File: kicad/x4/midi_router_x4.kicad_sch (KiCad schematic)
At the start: 83 parts, among them J1 USB_B, J11 DIN-5_180degree, J12 DIN-5_180degree, J13 DIN-5_180degree, J14 DIN-5_180degree, J2 Conn_02x03_Odd_Even, J21 DIN-5_180degree, J22 DIN-5_180degree, J23 DIN-5_180degree, J24 DIN-5_180degree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

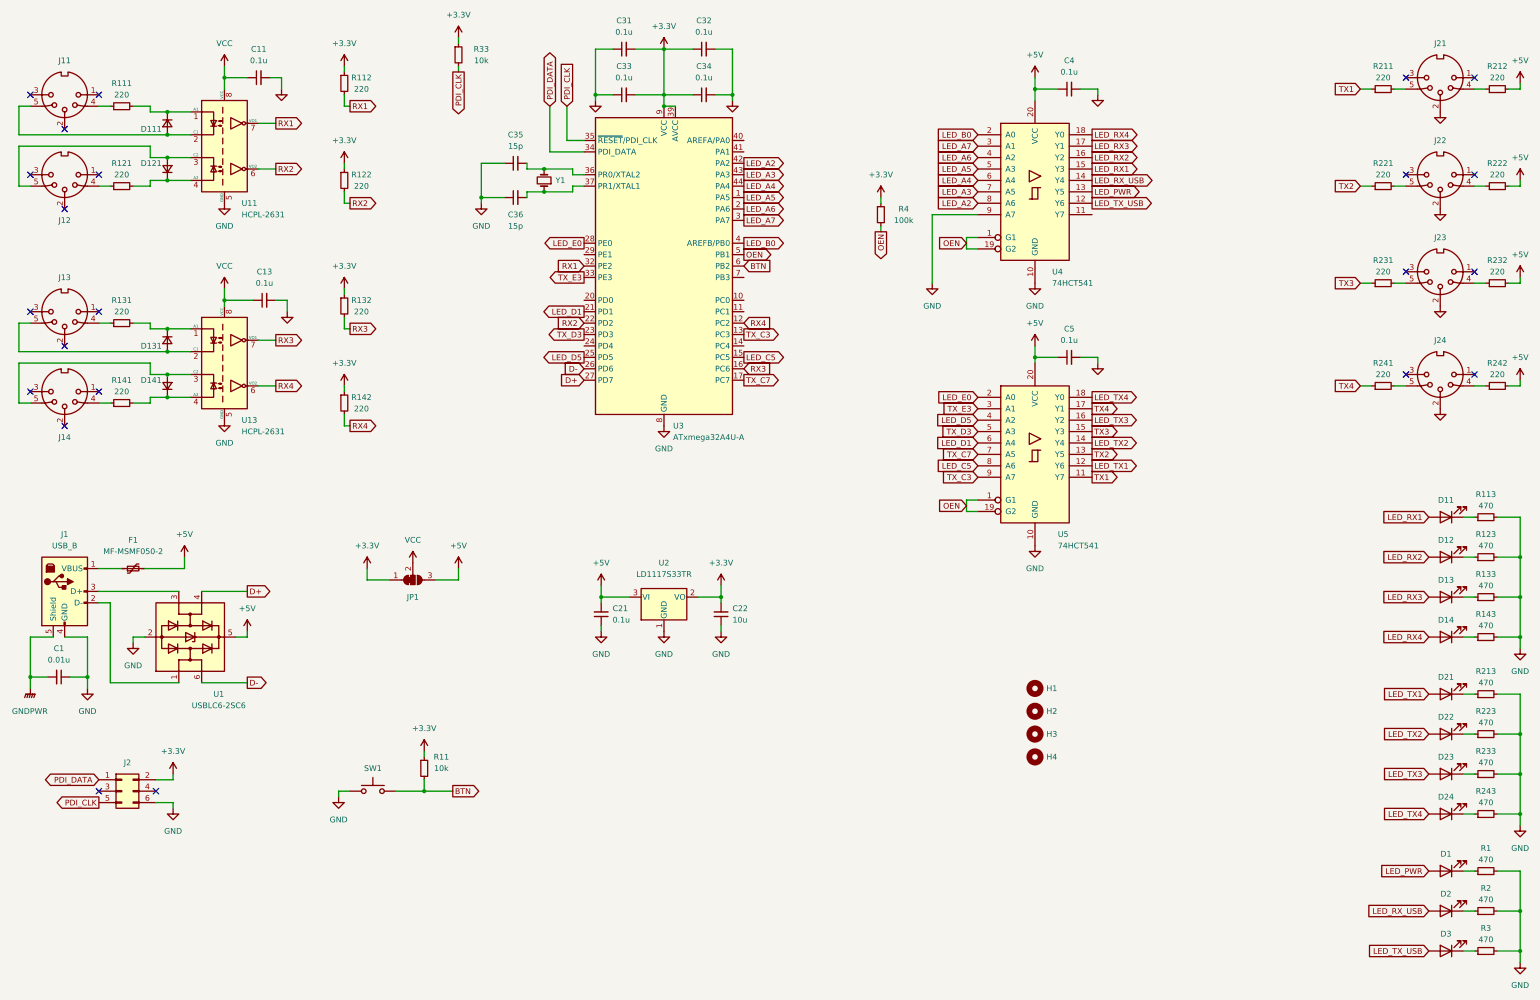
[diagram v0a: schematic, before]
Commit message: x4 KiCad upgrade
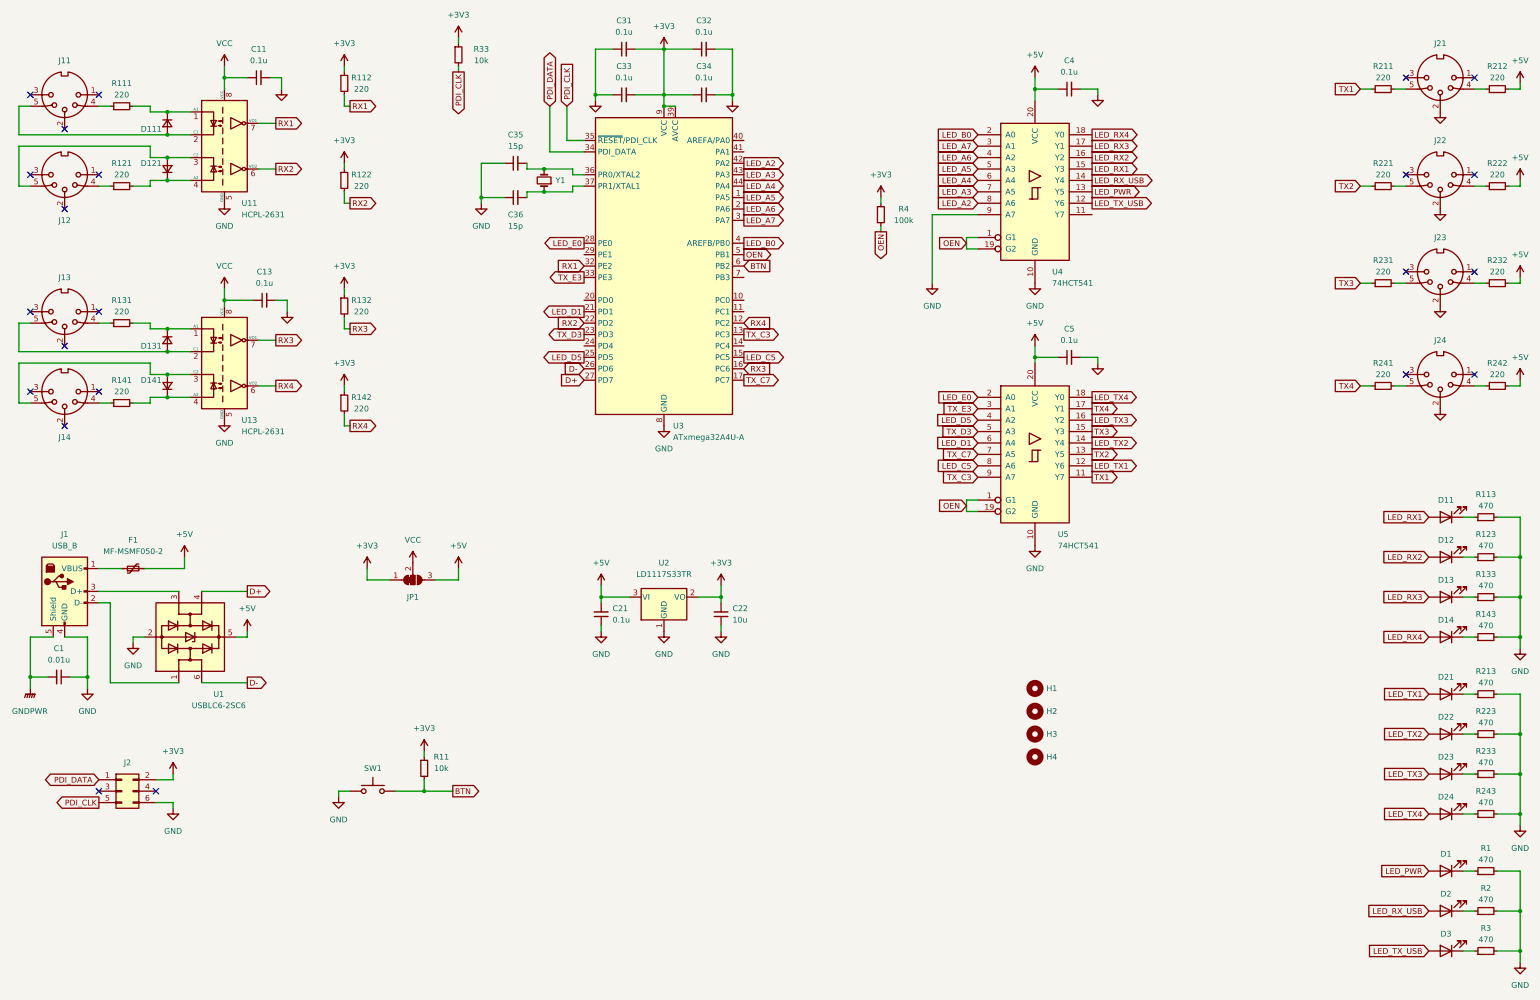
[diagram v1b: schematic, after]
